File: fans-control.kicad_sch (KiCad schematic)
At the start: 53 parts, among them J2 PinHeader_1x4_P2.5mm_Drill1mm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, J3 PinHeader_1x4_P2.5mm_Drill1mm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, J4 PinHeader_1x4_P2.5mm_Drill1mm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, J5 PinHeader_1x4_P2.5mm_Drill1mm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, Q2 2N7002K-T1-E3, Q3 BSS138PW, U5 LM339_TSSOP_Split, U6 TS5A3359_VSSOP, U7 74CBTLV3257_VQFN, U8 74VHC153FT

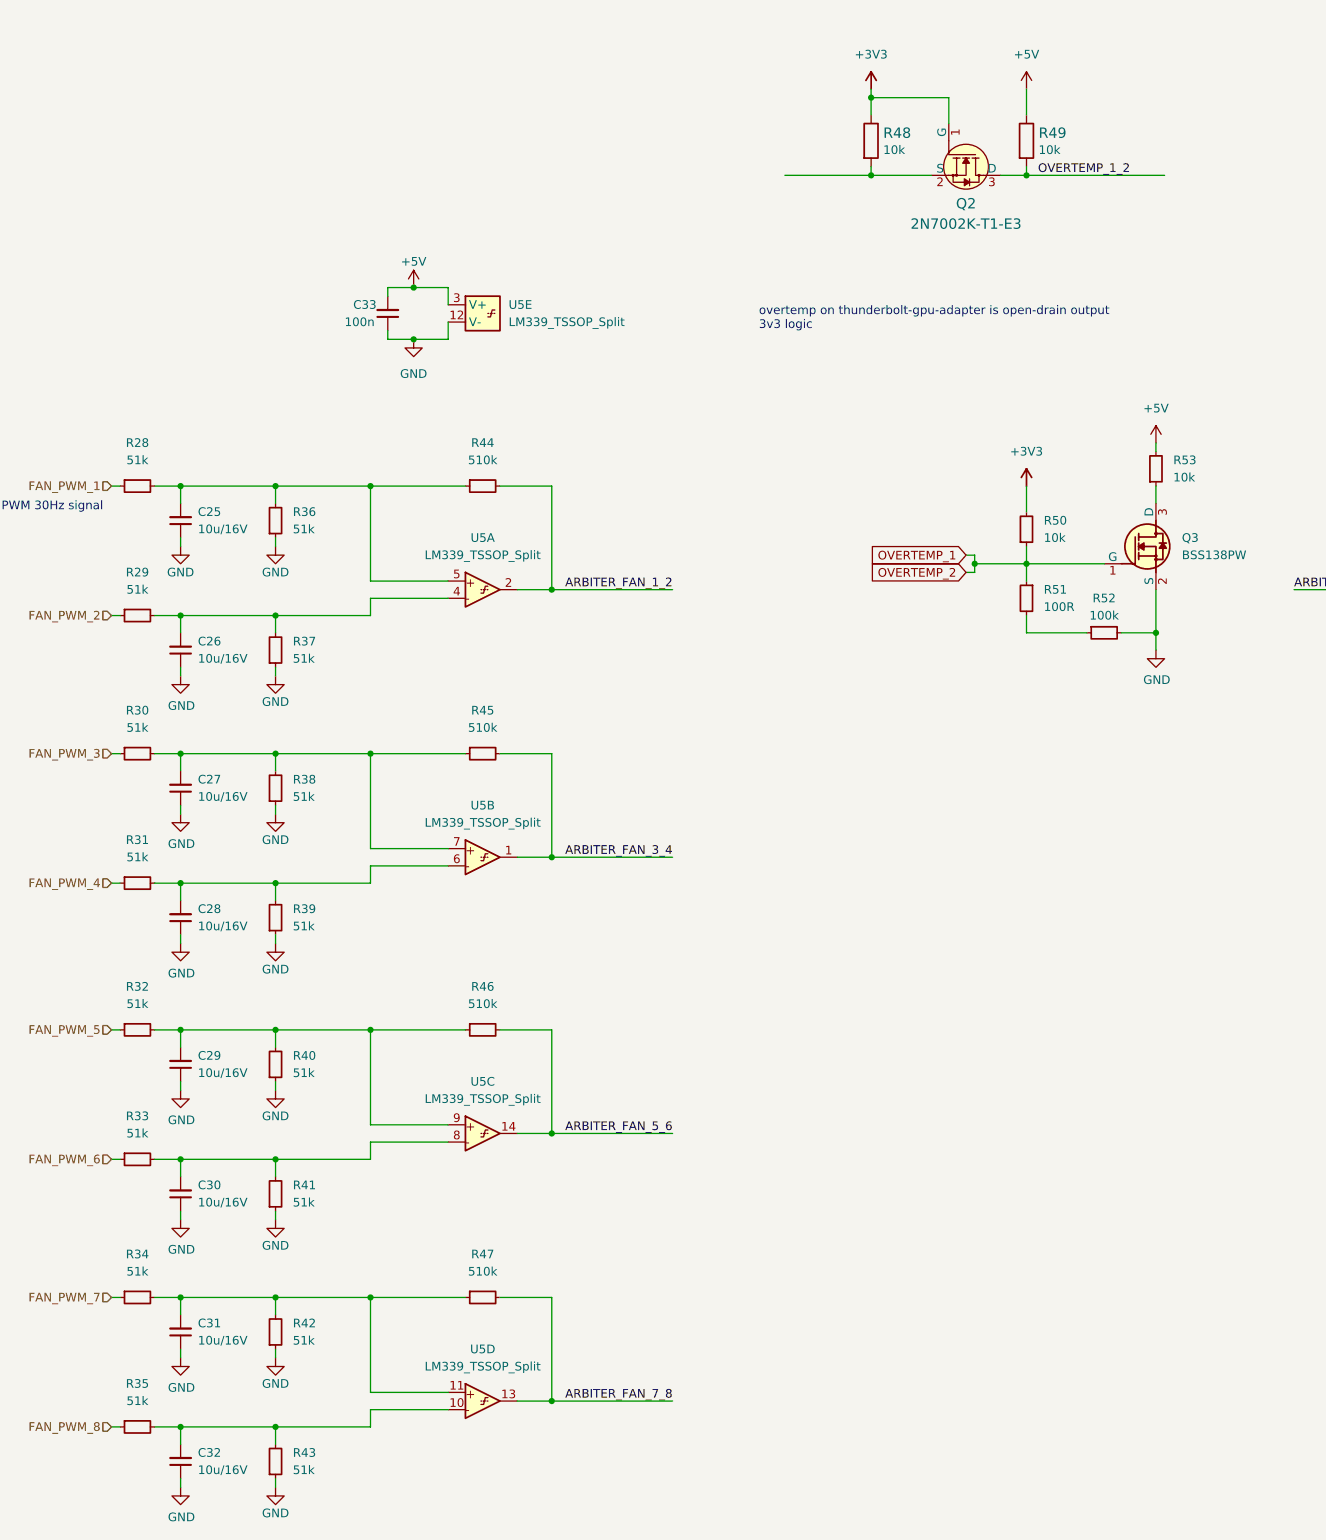
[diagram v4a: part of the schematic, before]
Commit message: Standarize debug signal schematic
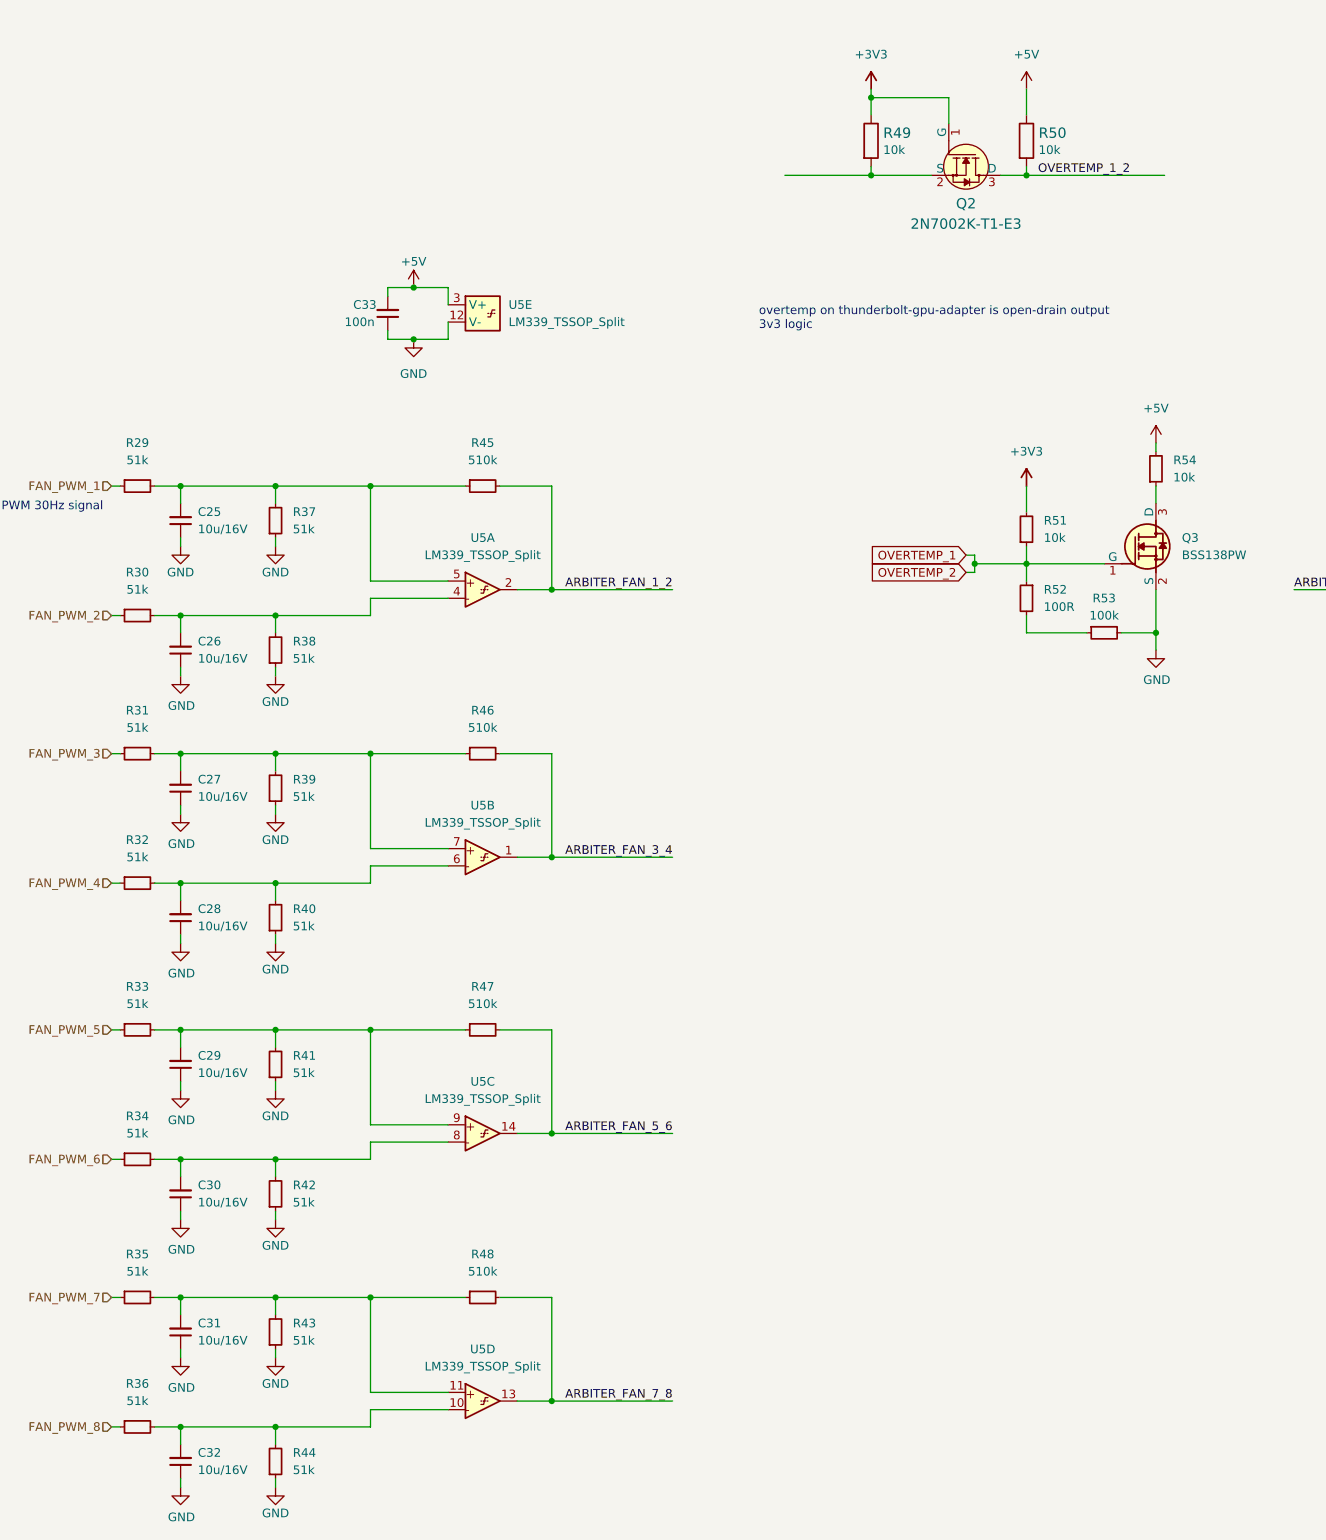
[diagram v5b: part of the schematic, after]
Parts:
- renumbered R28 to R29, R29 to R30, R30 to R31, R31 to R32, R32 to R33, R33 to R34, R34 to R35, R35 to R36, R36 to R37, R37 to R38, R38 to R39, R39 to R40, R40 to R41, R41 to R42, R42 to R43, R43 to R44, R44 to R45, R45 to R46, R46 to R47, R47 to R48, R48 to R49, R49 to R50, R50 to R51, R51 to R52, R52 to R53, R53 to R54
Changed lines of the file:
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@@
   (symbol (lib_id "antmicroResistors0402:R_51k_0402") (at 69.85 125.73 90) (unit 1)
     (in_bom yes) (on_board yes) (fields_autoplaced)
-    (property "Reference" "R39" (id 0) (at 72.39 121.9199 90)
+    (property "Reference" "R40" (id 0) (at 72.39 121.9199 90)
       (effects (font (size 1.27 1.27) (thickness 0.15)) (justify right))
     )
@@
   (symbol (lib_id "antmicroResistors0402:R_51k_0402") (at 46.99 118.11 0) (unit 1)
     (in_bom yes) (on_board yes) (fields_autoplaced)
-    (property "Reference" "R31" (id 0) (at 49.53 111.76 0)
+    (property "Reference" "R32" (id 0) (at 49.53 111.76 0)
       (effects (font (size 1.27 1.27) (thickness 0.15)))
     )
@@
   (symbol (lib_id "antmicroResistors0402:R_10k_0402") (at 157.48 8.89 270) (unit 1)
     (in_bom yes) (on_board yes)
-    (property "Reference" "R48" (id 0) (at 159.258 7.747 90)
+    (property "Reference" "R49" (id 0) (at 159.258 7.747 90)
       (effects (font (size 1.524 1.524)) (justify left))
     )
@@
   (symbol (lib_id "antmicroResistors0402:R_51k_0402") (at 46.99 78.74 0) (unit 1)
     (in_bom yes) (on_board yes) (fields_autoplaced)
-    (property "Reference" "R29" (id 0) (at 49.53 72.39 0)
+    (property "Reference" "R30" (id 0) (at 49.53 72.39 0)
       (effects (font (size 1.27 1.27) (thickness 0.15)))
     )
@@
   (symbol (lib_name "R_10k_0402_1") (lib_id "antmicroResistors0402:R_10k_0402") (at 180.34 68.58 90) (unit 1)
     (in_bom yes) (on_board yes) (fields_autoplaced)
-    (property "Reference" "R50" (id 0) (at 182.88 64.7699 90)
+    (property "Reference" "R51" (id 0) (at 182.88 64.7699 90)
       (effects (font (size 1.27 1.27) (thickness 0.15)) (justify right))
     )
@@
   (symbol (lib_id "antmicroResistors0402:R_51k_0402") (at 46.99 99.06 0) (unit 1)
     (in_bom yes) (on_board yes) (fields_autoplaced)
-    (property "Reference" "R30" (id 0) (at 49.53 92.71 0)
+    (property "Reference" "R31" (id 0) (at 49.53 92.71 0)
       (effects (font (size 1.27 1.27) (thickness 0.15)))
     )
@@
   (symbol (lib_name "R_10k_0402_1") (lib_id "antmicroResistors0402:R_10k_0402") (at 199.39 59.69 90) (unit 1)
     (in_bom yes) (on_board yes) (fields_autoplaced)
-    (property "Reference" "R53" (id 0) (at 201.93 55.8799 90)
+    (property "Reference" "R54" (id 0) (at 201.93 55.8799 90)
       (effects (font (size 1.27 1.27) (thickness 0.15)) (justify right))
     )
@@
   (symbol (lib_id "antmicroResistors0402:R_510k_0402") (at 97.79 99.06 0) (unit 1)
     (in_bom yes) (on_board yes) (fields_autoplaced)
-    (property "Reference" "R45" (id 0) (at 100.33 92.71 0)
+    (property "Reference" "R46" (id 0) (at 100.33 92.71 0)
       (effects (font (size 1.27 1.27) (thickness 0.15)))
     )
@@
   (symbol (lib_id "antmicroResistors0402:R_51k_0402") (at 46.99 59.69 0) (unit 1)
     (in_bom yes) (on_board yes) (fields_autoplaced)
-    (property "Reference" "R28" (id 0) (at 49.53 53.34 0)
+    (property "Reference" "R29" (id 0) (at 49.53 53.34 0)
       (effects (font (size 1.27 1.27) (thickness 0.15)))
     )
@@
   (symbol (lib_id "antmicroResistors0402:R_510k_0402") (at 97.79 179.07 0) (unit 1)
     (in_bom yes) (on_board yes) (fields_autoplaced)
-    (property "Reference" "R47" (id 0) (at 100.33 172.72 0)
+    (property "Reference" "R48" (id 0) (at 100.33 172.72 0)
       (effects (font (size 1.27 1.27) (thickness 0.15)))
     )
@@
   (symbol (lib_id "antmicroResistors0402:R_510k_0402") (at 97.79 59.69 0) (unit 1)
     (in_bom yes) (on_board yes) (fields_autoplaced)
-    (property "Reference" "R44" (id 0) (at 100.33 53.34 0)
+    (property "Reference" "R45" (id 0) (at 100.33 53.34 0)
       (effects (font (size 1.27 1.27) (thickness 0.15)))
     )
@@
   (symbol (lib_id "antmicroResistors0402:R_51k_0402") (at 69.85 86.36 90) (unit 1)
     (in_bom yes) (on_board yes) (fields_autoplaced)
-    (property "Reference" "R37" (id 0) (at 72.39 82.5499 90)
+    (property "Reference" "R38" (id 0) (at 72.39 82.5499 90)
       (effects (font (size 1.27 1.27) (thickness 0.15)) (justify right))
     )
@@
   (symbol (lib_id "antmicroResistors0402:R_51k_0402") (at 69.85 147.32 90) (unit 1)
     (in_bom yes) (on_board yes) (fields_autoplaced)
-    (property "Reference" "R40" (id 0) (at 72.39 143.5099 90)
+    (property "Reference" "R41" (id 0) (at 72.39 143.5099 90)
       (effects (font (size 1.27 1.27) (thickness 0.15)) (justify right))
     )
@@
   (symbol (lib_id "antmicroResistors0402:R_100k_0402") (at 189.23 81.28 0) (unit 1)
     (in_bom yes) (on_board yes) (fields_autoplaced)
-    (property "Reference" "R52" (id 0) (at 191.77 76.2 0)
+    (property "Reference" "R53" (id 0) (at 191.77 76.2 0)
       (effects (font (size 1.27 1.27) (thickness 0.15)))
     )
@@
   (symbol (lib_id "antmicroResistors0402:R_100R_0402") (at 180.34 73.66 270) (unit 1)
     (in_bom yes) (on_board yes) (fields_autoplaced)
-    (property "Reference" "R51" (id 0) (at 182.88 74.9299 90)
+    (property "Reference" "R52" (id 0) (at 182.88 74.9299 90)
       (effects (font (size 1.27 1.27) (thickness 0.15)) (justify left))
     )
@@
   (symbol (lib_id "antmicroResistors0402:R_51k_0402") (at 69.85 205.74 90) (unit 1)
     (in_bom yes) (on_board yes) (fields_autoplaced)
-    (property "Reference" "R43" (id 0) (at 72.39 201.9299 90)
+    (property "Reference" "R44" (id 0) (at 72.39 201.9299 90)
       (effects (font (size 1.27 1.27) (thickness 0.15)) (justify right))
     )
@@
   (symbol (lib_id "antmicroResistors0402:R_510k_0402") (at 97.79 139.7 0) (unit 1)
     (in_bom yes) (on_board yes) (fields_autoplaced)
-    (property "Reference" "R46" (id 0) (at 100.33 133.35 0)
+    (property "Reference" "R47" (id 0) (at 100.33 133.35 0)
       (effects (font (size 1.27 1.27) (thickness 0.15)))
     )
@@
   (symbol (lib_id "antmicroResistors0402:R_10k_0402") (at 180.34 8.89 270) (unit 1)
     (in_bom yes) (on_board yes)
-    (property "Reference" "R49" (id 0) (at 182.118 7.747 90)
+    (property "Reference" "R50" (id 0) (at 182.118 7.747 90)
       (effects (font (size 1.524 1.524)) (justify left))
     )
@@
   (symbol (lib_id "antmicroResistors0402:R_51k_0402") (at 46.99 158.75 0) (unit 1)
     (in_bom yes) (on_board yes) (fields_autoplaced)
-    (property "Reference" "R33" (id 0) (at 49.53 152.4 0)
+    (property "Reference" "R34" (id 0) (at 49.53 152.4 0)
       (effects (font (size 1.27 1.27) (thickness 0.15)))
     )
@@
   (symbol (lib_id "antmicroResistors0402:R_51k_0402") (at 69.85 186.69 90) (unit 1)
     (in_bom yes) (on_board yes) (fields_autoplaced)
-    (property "Reference" "R42" (id 0) (at 72.39 182.8799 90)
+    (property "Reference" "R43" (id 0) (at 72.39 182.8799 90)
       (effects (font (size 1.27 1.27) (thickness 0.15)) (justify right))
     )
@@
   (symbol (lib_id "antmicroResistors0402:R_51k_0402") (at 46.99 139.7 0) (unit 1)
     (in_bom yes) (on_board yes) (fields_autoplaced)
-    (property "Reference" "R32" (id 0) (at 49.53 133.35 0)
+    (property "Reference" "R33" (id 0) (at 49.53 133.35 0)
       (effects (font (size 1.27 1.27) (thickness 0.15)))
     )
@@
   (symbol (lib_id "antmicroResistors0402:R_51k_0402") (at 46.99 198.12 0) (unit 1)
     (in_bom yes) (on_board yes) (fields_autoplaced)
-    (property "Reference" "R35" (id 0) (at 49.53 191.77 0)
+    (property "Reference" "R36" (id 0) (at 49.53 191.77 0)
       (effects (font (size 1.27 1.27) (thickness 0.15)))
     )
@@
   (symbol (lib_id "antmicroResistors0402:R_51k_0402") (at 46.99 179.07 0) (unit 1)
     (in_bom yes) (on_board yes) (fields_autoplaced)
-    (property "Reference" "R34" (id 0) (at 49.53 172.72 0)
+    (property "Reference" "R35" (id 0) (at 49.53 172.72 0)
       (effects (font (size 1.27 1.27) (thickness 0.15)))
     )
@@
   (symbol (lib_id "antmicroResistors0402:R_51k_0402") (at 69.85 106.68 90) (unit 1)
     (in_bom yes) (on_board yes) (fields_autoplaced)
-    (property "Reference" "R38" (id 0) (at 72.39 102.8699 90)
+    (property "Reference" "R39" (id 0) (at 72.39 102.8699 90)
       (effects (font (size 1.27 1.27) (thickness 0.15)) (justify right))
     )
@@
   (symbol (lib_id "antmicroResistors0402:R_51k_0402") (at 69.85 67.31 90) (unit 1)
     (in_bom yes) (on_board yes) (fields_autoplaced)
-    (property "Reference" "R36" (id 0) (at 72.39 63.4999 90)
+    (property "Reference" "R37" (id 0) (at 72.39 63.4999 90)
       (effects (font (size 1.27 1.27) (thickness 0.15)) (justify right))
     )
@@
   (symbol (lib_id "antmicroResistors0402:R_51k_0402") (at 69.85 166.37 90) (unit 1)
     (in_bom yes) (on_board yes) (fields_autoplaced)
-    (property "Reference" "R41" (id 0) (at 72.39 162.5599 90)
-      (effects (font (size 1.27 1.27) (thickness 0.15)) (justify right))
-    )
+    (property "Reference" "R42" (id 0) (at 72.39 162.5599 90)
+      (effects (font (size 1.27 1.27) (thickness 0.15)) (justify right))
+    )

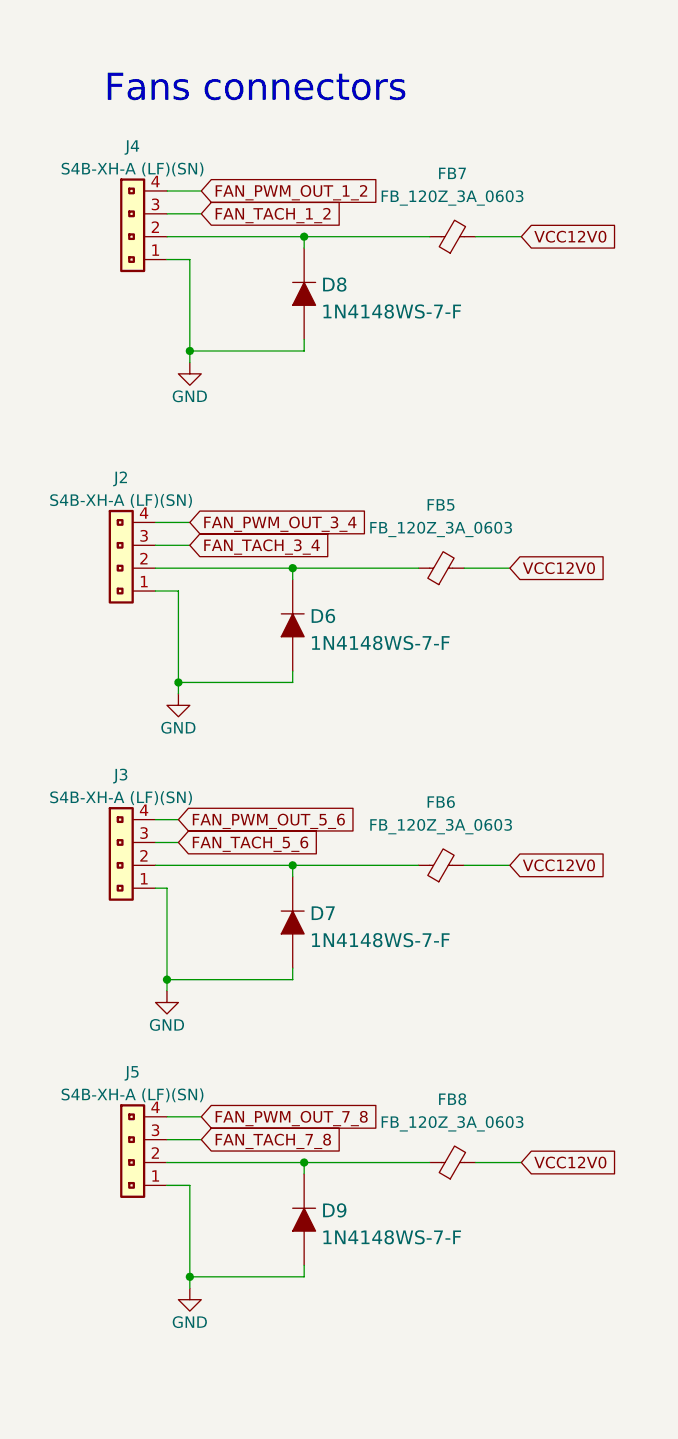
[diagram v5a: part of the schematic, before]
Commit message: Standarize fans control
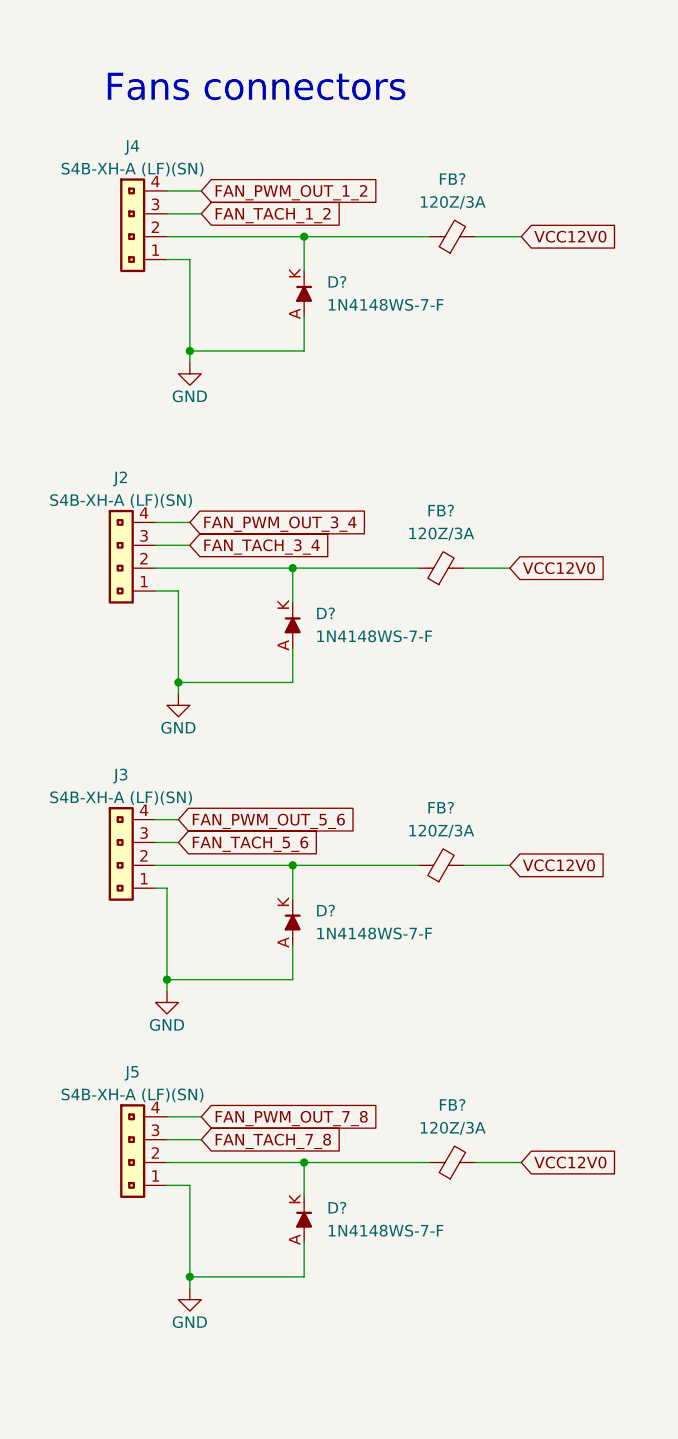
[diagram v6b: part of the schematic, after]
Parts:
- removed D6, D7, D8, D9: 1N4148WS-7-F, antmicro-footprints:SOD-323, symbol antmicroDiodesRectifiersSingle:1N4148WS-7-F
- removed FB5, FB6, FB7, FB8: FB_120Z_3A_0603, antmicro-footprints:FB_0603_1608Metric, symbol antmicroFerriteBeadsandChips:FB_120Z_3A_0603
- added D? (x4): 1N4148WS-7-F, antmicro-footprints:SOD-323, symbol antmicroDiodesRectifiersSingle:1N4148WS-7-F
- added FB? (x4): FB_120Z_3A_Murata-BLM18SG_0603, antmicro-footprints:FB_0603_1608Metric, symbol antmicroFerriteBeadsandChips:FB_120Z_3A_Murata-BLM18SG_0603
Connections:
- net GND: now also D?.A, D?.A, D?.A, D?.A
- net VCC12V0: now also FB?.2, FB?.2, FB?.2, FB?.2
- net at J5.2: now also D?.K, FB?.1
- net at J3.2: now also D?.K, FB?.1
- net at J2.2: now also D?.K, FB?.1
- net at J4.2: now also D?.K, FB?.1
